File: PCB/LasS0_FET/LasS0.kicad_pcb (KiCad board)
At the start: 2 copper layers, 29.3 x 82 mm, 42 parts, among them J1 CiKe2PinSock, J2 CiKe2PinSock, J3 CiKe2PinSock, J4 CiKe2PinSock, Q1 AO3400A, Q2 AO3400A, U1 TPS54331D, U2 EL817S1

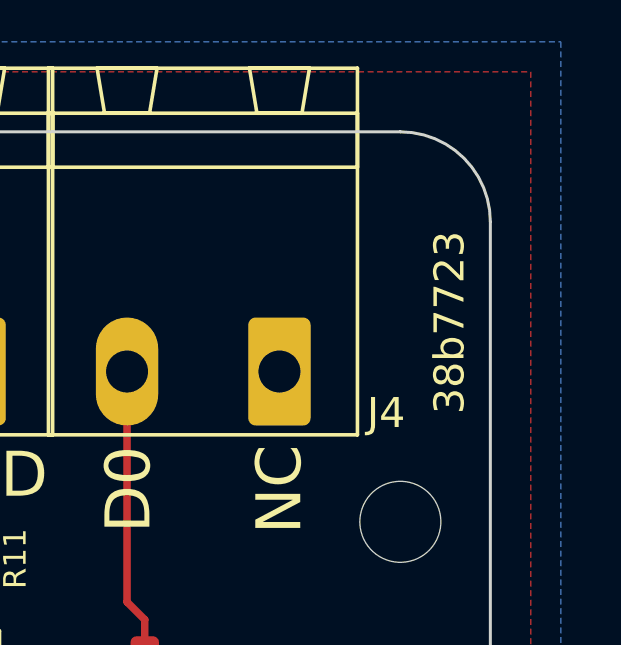
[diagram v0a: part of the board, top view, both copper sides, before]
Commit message: [PCB] update silkscreen documentation, changing GitHub to GitLab
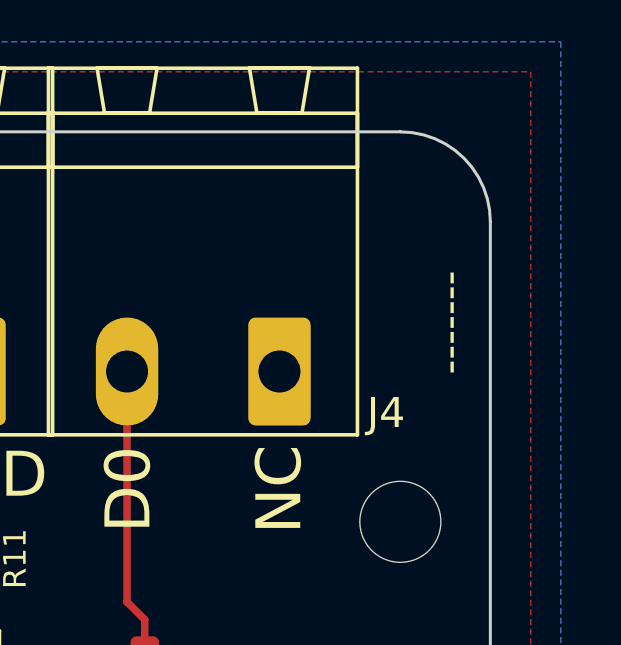
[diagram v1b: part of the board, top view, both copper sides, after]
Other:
- board text added: "-------"
- board text added: "Logic level impulse to S0 converter Chrismettal 2021_06 GitLab.com/Chrismettal/LasS0"
- board text removed: "38b7723"
- board text removed: "Logic level impulse to S0 converter Chrismettal 2021_06 github.com/Chrismettal/LasS0"
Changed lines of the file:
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@@
-(kicad_pcb (version 20210424) (generator pcbnew)
+(kicad_pcb (version 20210623) (generator pcbnew)
   (general
     (thickness 1.6)
@@
     (effects (font (size 3 3) (thickness 0.75) italic) (justify mirror))
   )
-  (gr_text "Logic level impulse to S0 converter\n\nChrismettal 2021_06\ngithub.com/Chrismettal/LasS0" (at 150.415 100 90) (layer "B.SilkS")
+  (gr_text "Logic level impulse to S0 converter\n\nChrismettal 2021_06\nGitLab.com/Chrismettal/LasS0" (at 150.415 100 90) (layer "B.SilkS")
     (effects (font (size 2 2) (thickness 0.3)) (justify mirror))
   )
@@
     (effects (font (size 1.5 1.5) (thickness 0.25)))
   )
-  (gr_text "38b7723\n" (at 161.8 65.356 90) (layer "F.SilkS")
+  (gr_text "-------" (at 161.8 65.356 90) (layer "F.SilkS")
     (effects (font (size 1 1) (thickness 0.15)))
   )
